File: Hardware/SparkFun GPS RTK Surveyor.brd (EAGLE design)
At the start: 69.1 x 109.1 mm, 167 parts, among them J2 CONN_04, J3 USB-C, J4 Qwiic Right Angle, J6 Start Base, J7 Power Switch, J9 CONN_04, Q2 MBT3904DW1T1, U1 MCP73831, U2 3.3V, U3 ZED-F9P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

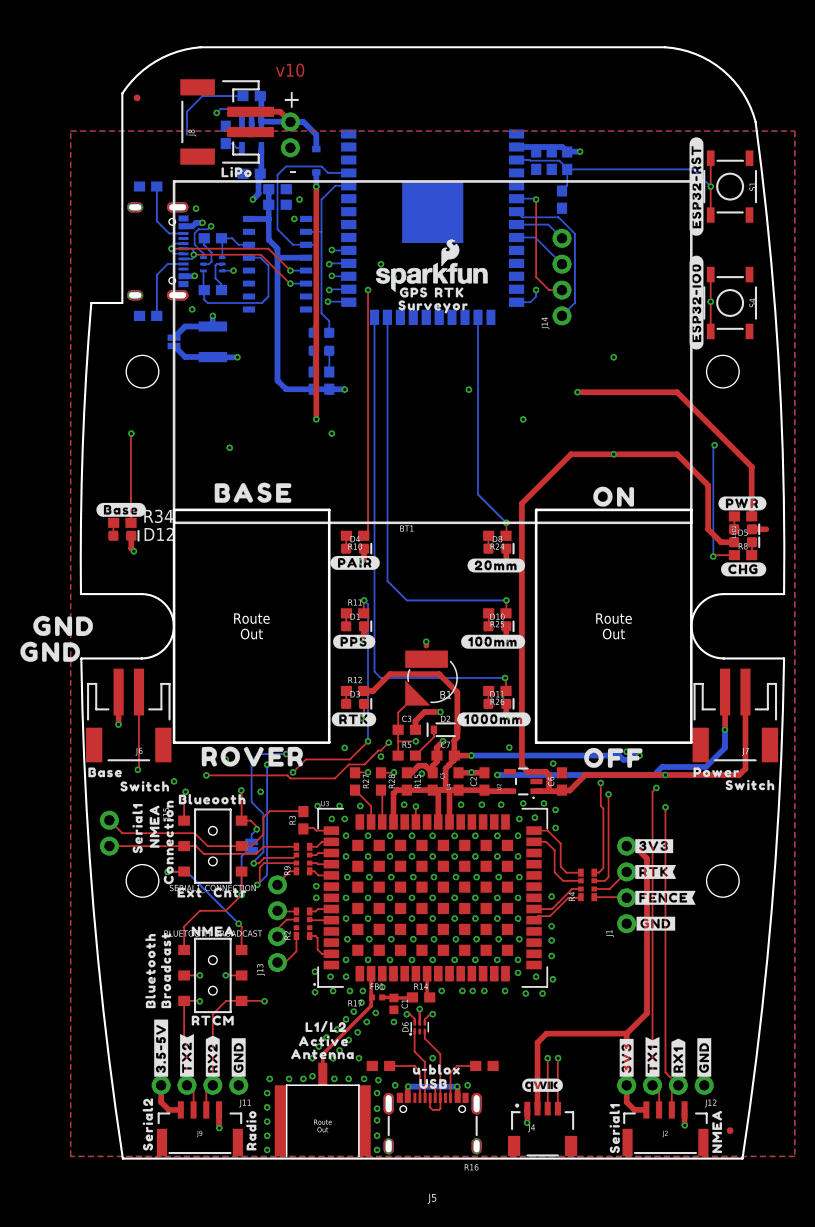
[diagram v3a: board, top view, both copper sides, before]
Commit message: v11 add microSD. Fix power switch. Fix BT switch. Add I2C. Remove old files. Add enclsoure cut files.
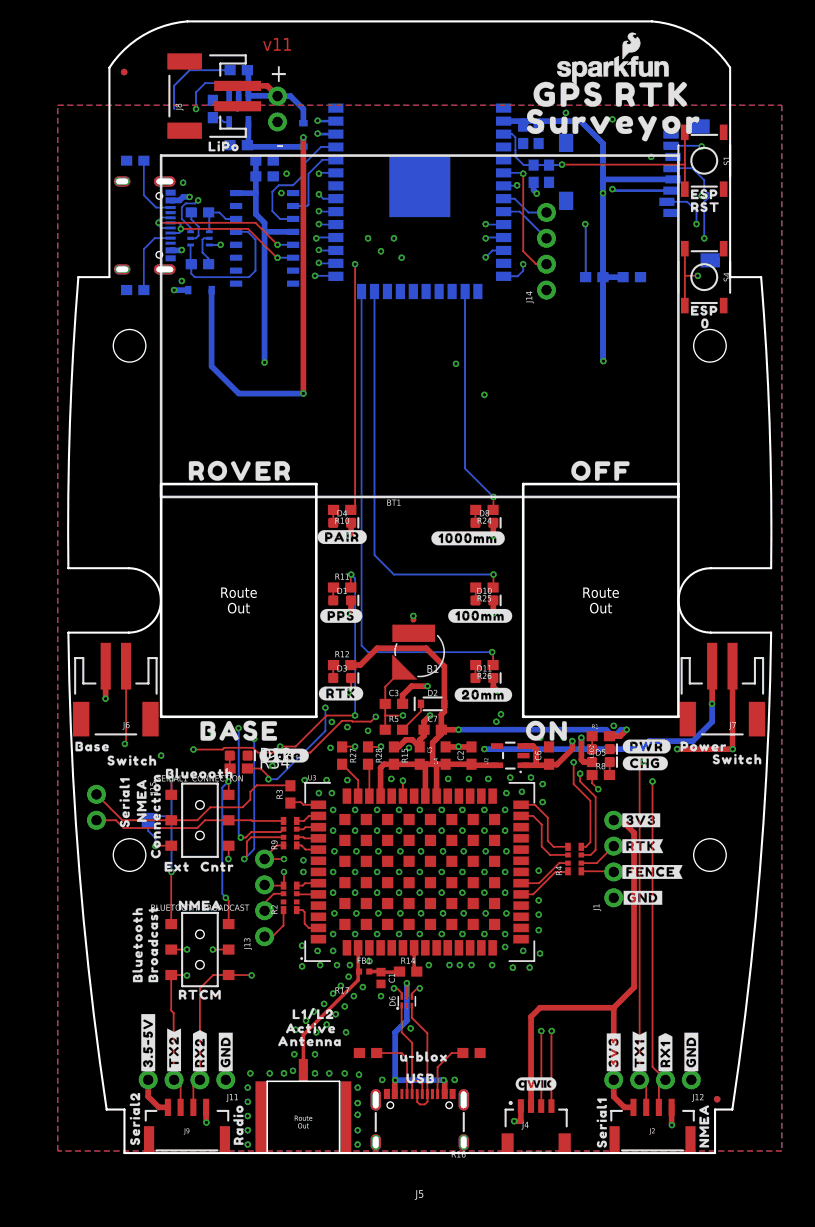
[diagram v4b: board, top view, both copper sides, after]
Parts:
- removed BYP: JUMPER-SMT_2_NO_SILK, SparkFun-Jumpers:SMT-JUMPER_2_NO_SILK
- removed D15: Yellow, SparkFun-LED:LED-0603
- removed F1: 6V/2A, SparkFun-Fuses:1210
- removed LED1: GREEN, SparkFun-LED:LED-0603
- removed R33: 1k, SparkFun-Resistors:0603
- removed R36: 330, SparkFun-Resistors:0603
- removed U$69: (no value), output:#BYP#0
- added C16: 0.1uF, SparkFun-Capacitors:0603
- added D9: 3A/10V/280mV, SparkFun-DiscreteSemi:SOD-323
- added J17: MICRO-SD, SparkFun-Connectors:MICRO-SD-SOCKET
- added R13: 100k, SparkFun-Resistors:0603
- added U$72: (no value), output:#TX#1
- added U$73: (no value), output:#DUAL#0
- added U$74: (no value), output:ESP0
- D10, D11, D8: value BLUE -> GREEN
- D12: value BLUE -> RED
- D3: value GREEN -> WHITE
- R7: value 2.2k -> 1k
- U$14: device output:SURVEYOR1 -> output:#RX#2
- U$16: device output:RTK1 -> output:ZED0
- U$5: device output:GPS0 -> output:ESP0
- U$60: device output:#ESP32#IO0#0 -> output:RST1
- U$65: device output:#ESP32#RST#0 -> output:02
- U$70: device output:GND0 -> output:GPS_RTK0
- U$71: device output:GND0 -> output:_SURVEYOR3
- moved U$70 71.4 mm to (34.8, 104.3)
- moved U$71 71.2 mm to (33.3, 101.6)
- moved U$16 61.0 mm to (-4.57, 32.1), flipped to the bottom, turned to 90 degrees
- moved U$14 58.7 mm to (-6.35, 32.5), flipped to the bottom, turned to 270 degrees
- moved U$4 29.0 mm to (9.65, 39.4)
- moved U$5 28.6 mm to (51.3, 83.1)
- moved U$31 28.2 mm to (38.9, 67.3)
- moved U$44 28.1 mm to (1.27, 67.3)
- moved LOGO3 27.0 mm to (44.5, 106.7)
- moved R34 26.7 mm to (7.62, 38.1)
- moved D5 25.7 mm to (43.2, 38.7)
- moved R1 25.7 mm to (43.2, 41.3)
- moved U$13 25.7 mm to (43.2, 39.4)
- moved LED2 25.7 mm to (43.2, 40.0)
- moved R8 25.7 mm to (43.2, 37.5)
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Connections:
- net ESP32_13/POSACC1 renamed ESP32_13/POSACC3
- net ESP32_2/POSACC3 renamed ESP32_2/POSACC1
- removed net ESP32_IO21_SDA: U5.33
- removed net ESP32_IO22_SCL: U5.36
- removed net ESP32_IO25: U5.10
- removed net ESP32_IO26: U5.11
- removed net ESP32_IO27: U5.12
- removed net N$28: LED1.A, R36.1
- removed net N$31: D15.A, R33.1
- removed net TX_READY: J13.4, R9.P8
- removed net VBATT_SWTICHED: D7.C, J7.2
- removed net ZED_!RESET!: J13.3, R2.P5
- new net ESP32_IO25/!CS!: J17.CS, R13.1, U5.10
- new net ESP32_IO26/TX_READY: J13.4, R9.P8, U5.11
- new net ESP32_IO27/ZED-!RESET!: J13.3, R2.P5, U5.12
- new net VIN: C9.1, D5.A, D6.5, D7.C, D9.C, J5.VBUS1, J5.VBUS2, J7.2, U1.4
- net 3.3V: now also C16.1, J17.VCC, R13.2; no longer R33.2, R36.2
- net 5V: no longer BYP.2, C9.1, D5.A, D6.5, F1.2, J5.VBUS1, J5.VBUS2, U1.4
- net ESP32_IO18_SCK0: now also J17.SCLK
- net ESP32_IO19_MISO0: now also J17.DO
- net ESP32_IO23_MOSI0: now also J17.DI
- net ESP32_RXI: no longer D15.C
- net ESP32_TXO: no longer LED1.C
- net GND: now also C16.2, J17.CD1, J17.GND
- net N$32: now also D9.A; no longer BYP.1, F1.1
- net SCL: now also U5.36
- net SDA: now also U5.33
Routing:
- net VIN: track 0.00 -> 211.0 mm, vias 0 -> 9
- net 5V: track 259.5 -> 119.3 mm, vias 8 -> 3
- net VBATT_SWTICHED: track 109.5 -> 0.00 mm, vias 5 -> 0
- net ESP32_IO26/TX_READY: track 0.00 -> 83.4 mm, vias 0 -> 3
- net ESP32_IO27/ZED-!RESET!: track 0.00 -> 81.5 mm, vias 0 -> 3
- net SCL: track 81.6 -> 149.9 mm, vias 4 -> 6
- net SDA: track 82.0 -> 139.4 mm, vias 4 -> 6
- net ESP32_IO18_SCK0: track 0.00 -> 51.4 mm, vias 0 -> 2
- net ESP32_IO19_MISO0: track 0.00 -> 49.7 mm, vias 0 -> 3
- net ESP32_IO23_MOSI0: track 0.00 -> 43.5 mm, vias 0 -> 3
- net ESP32_IO25/!CS!: track 0.00 -> 32.3 mm, vias 0 -> 3
- net CHG_LED: track 98.0 -> 119.7 mm, vias 4 -> 5
- net ESP32_EN: track 83.4 -> 67.9 mm
- net EXTERNAL_SERIAL1_TXO: track 79.6 -> 94.8 mm, vias 3 -> 2
- net ESP32_4/BASE_STAT: track 44.8 -> 58.4 mm
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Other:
- board size 69.1 x 109.1 mm -> 69.1 x 111.1 mm
- board text added: "-ND"
- board text added: "10.16mm / 0.4" is common"
- board text added: "12.7mm / 0.5" is common"
- board text added: "350-3725-ND (Flat $0.25)"
- board text added: "350-3726-ND (Flat $0.25)"
- board text added: "350-3738-ND (Dome $0.25)"
- board text added: "NA"
- board text added: "Pipe length: 12.08-12.85mm"
- board text added: "Thckness of top cover: 2.25mm"
- board text added: "v11"
- board text removed: "492-1341-ND"
- board text removed: "9.5mm / 0.375" is common"
- board text removed: "LFB037CTP-ND"
- board text removed: "Pipe length: 9.83-10.6mm"
- board text removed: "v10"

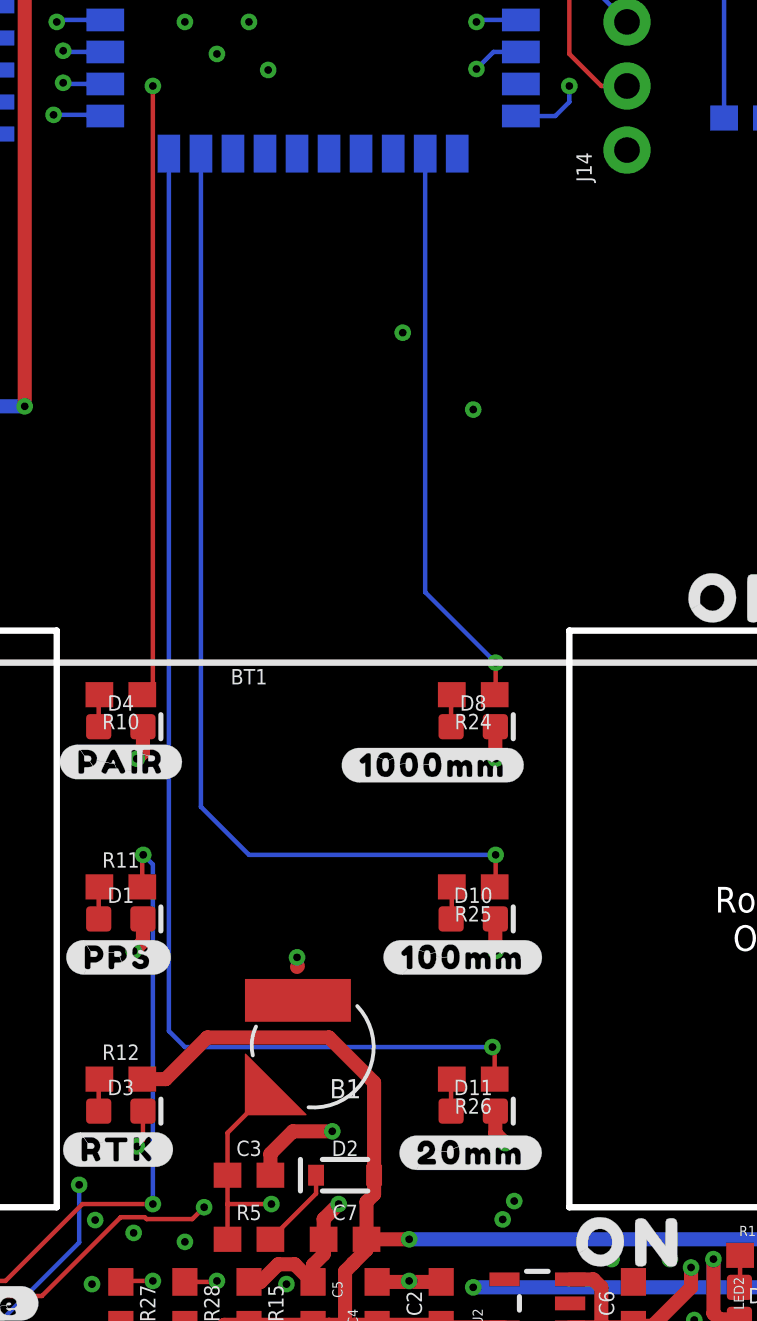
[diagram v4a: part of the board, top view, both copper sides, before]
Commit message: Change LED colors.
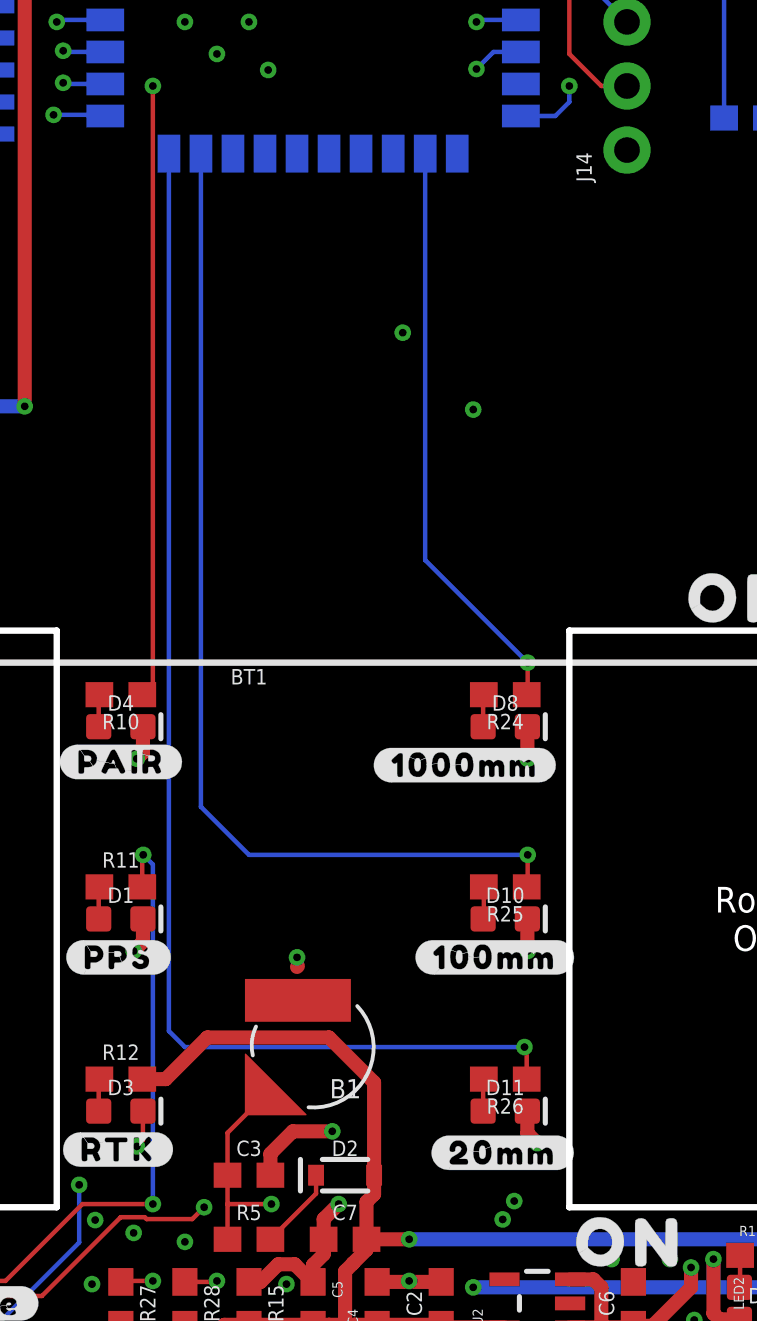
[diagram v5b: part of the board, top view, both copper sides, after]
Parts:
- moved D10 1.27 mm to (33.0, 54.6)
- moved D11 1.27 mm to (33.0, 47.0)
- moved D8 1.27 mm to (33.0, 62.2)
- moved R24 1.27 mm to (33.0, 63.5)
- moved R25 1.27 mm to (33.0, 55.9)
- moved R26 1.27 mm to (33.0, 48.3)
- moved U$66 1.27 mm to (30.1, 45.3)
- moved U$67 1.27 mm to (29.5, 53.1)
- moved U$68 1.27 mm to (27.8, 60.7)
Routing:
- net ESP32_2/POSACC1: track 49.2 -> 50.5 mm
- net ESP32_15/POSACC2: track 39.7 -> 40.9 mm
- net ESP32_13/POSACC3: track 22.6 -> 23.1 mm

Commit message: Update parts with prod_ids
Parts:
- J2, J9: value CONN_04 -> (none); device SparkFun GPS RTK Surveyor:JST-4-SMD-1.25MM-LOCKING -> SparkFun-Connectors:JST-4-SMD-1.25MM-LOCKING
- JP21, JP61, JP71, JP81: device SparkFun:MICRO-FIDUCIAL -> SparkFun-Aesthetics:FIDUCIAL-MICRO
- U3: value ZED-F9P -> U-BLOX_ZED-F9P; device ZED-F9P:ZED-F9P -> SparkFun-GPS:ZED-F9P

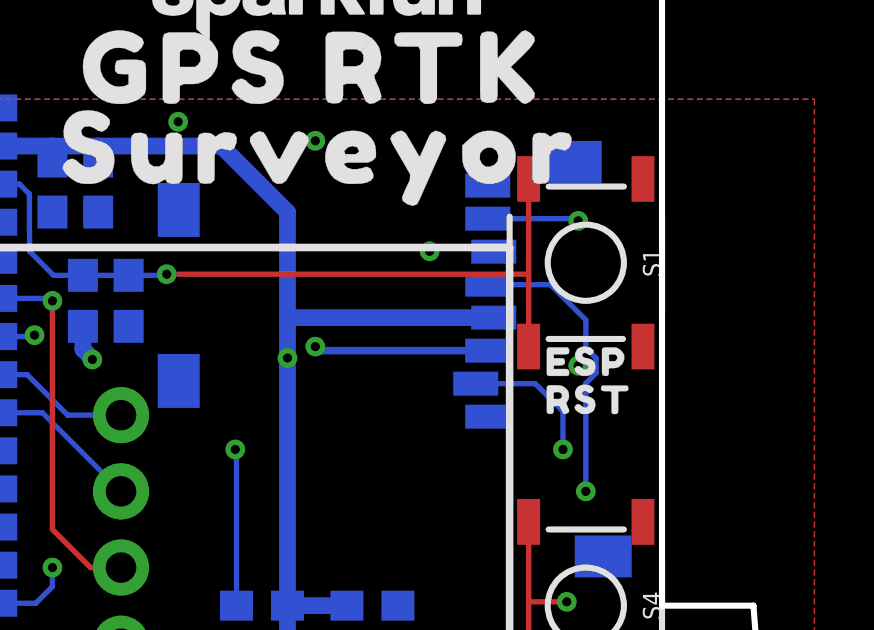
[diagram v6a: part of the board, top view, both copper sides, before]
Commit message: Update microSD socket
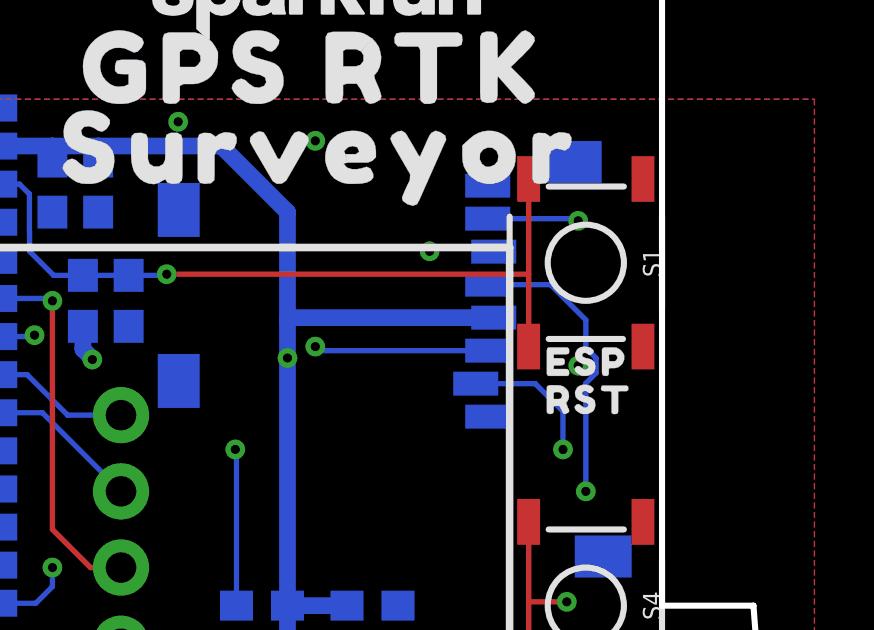
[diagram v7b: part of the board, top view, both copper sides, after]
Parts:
- J16: value MICRO-SD -> microSD
- renumbered J17 to J16
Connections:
- removed net ESP32_IO19_MISO0: J16.DO, U5.31
- removed net ESP32_IO23_MOSI0: J16.DI, U5.37
- new net ESP32_IO19_CIPO0: J16.DO/DAT0, U5.31
- new net ESP32_IO23_COPI0: J16.DI/CMD, U5.37
- net ESP32_IO25/!CS!: now also J16.CS/DAT3; no longer J16.CS
- net GND: now also J16.GND1, J16.GND3
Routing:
- net ESP32_IO19_CIPO0: track 0.00 -> 49.7 mm, vias 0 -> 3
- net ESP32_IO19_MISO0: track 49.7 -> 0.00 mm, vias 3 -> 0
- net ESP32_IO23_MOSI0: track 43.5 -> 0.00 mm, vias 3 -> 0
- net ESP32_IO23_COPI0: track 0.00 -> 43.5 mm, vias 0 -> 3
